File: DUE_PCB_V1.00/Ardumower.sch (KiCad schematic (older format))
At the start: 49 parts, among them J1 9V IN, J10 Sonar_R, J11 Sonar_C, J12 Sonar_L, J13 P_Right, J14 DS3231 RTC, J15 Button, J16 Button, J17 Button, J18 Button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

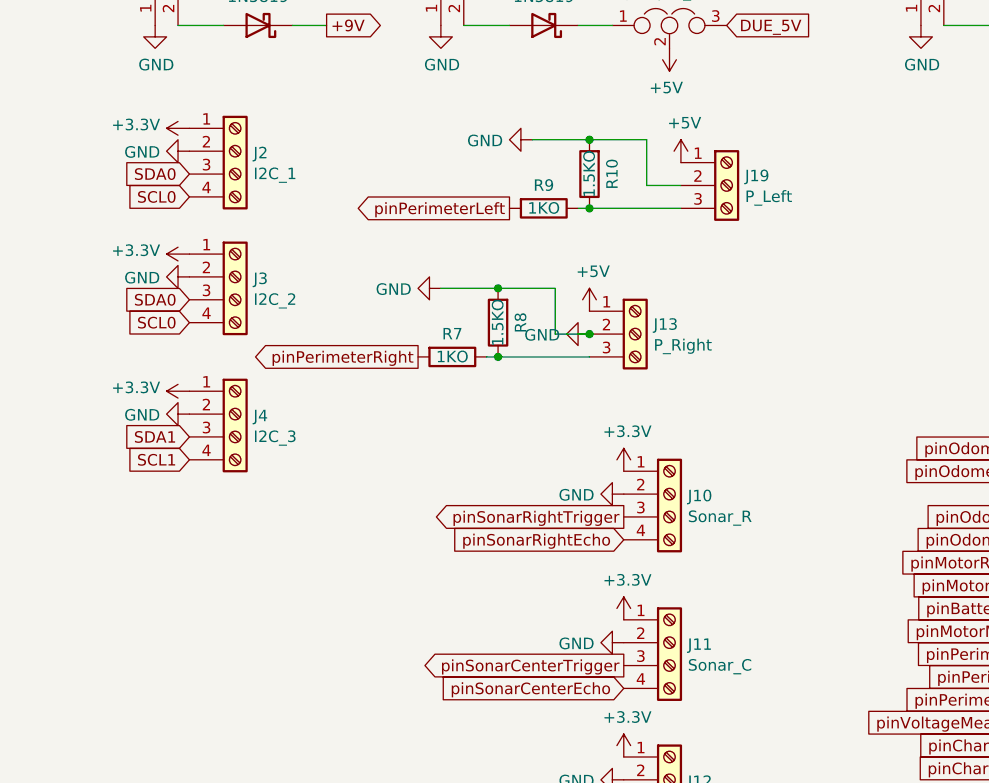
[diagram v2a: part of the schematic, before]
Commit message: Rename I2C Connectors
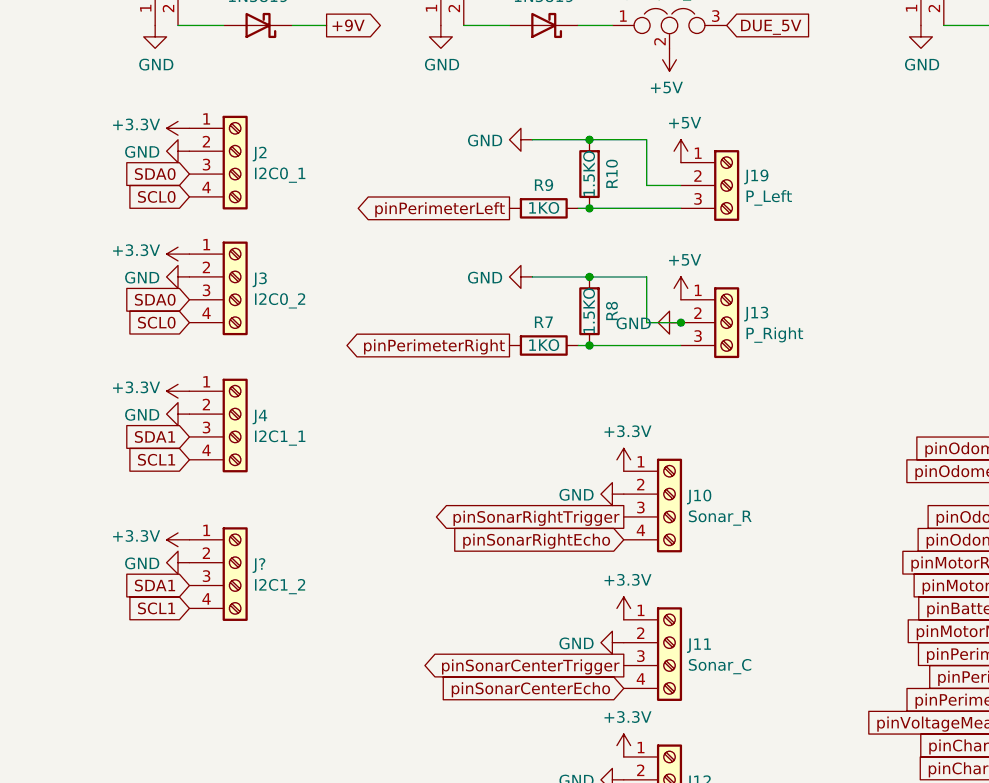
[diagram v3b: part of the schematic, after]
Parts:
- added J?: I2C1_2, Connector_PinHeader_2.54mm:PinHeader_1x04_P2.54mm_Vertical, symbol Connector:Screw_Terminal_01x04
- J2: value I2C_1 -> I2C0_1
- J3: value I2C_2 -> I2C0_2
- J4: value I2C_3 -> I2C1_1
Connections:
- net +3V3: now also J?.1 (Pin_1)
- net GND: now also J?.2 (Pin_2)
- net SCL1: now also J?.4 (Pin_4)
- net SDA1: now also J?.3 (Pin_3)
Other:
- moved on the sheet: J13, R7, R8
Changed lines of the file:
@@
 P 1150 1400
 F 0 "J2" H 1230 1392 50  0000 L CNN
-F 1 "I2C_1" H 1230 1301 50  0000 L CNN
+F 1 "I2C0_1" H 1230 1301 50  0000 L CNN
 F 2 "Connector_PinHeader_2.54mm:PinHeader_1x04_P2.54mm_Vertical" H 1150 1400 50  0001 C CNN
 F 3 "~" H 1150 1400 50  0001 C CNN
@@
 P 1150 1950
 F 0 "J3" H 1230 1942 50  0000 L CNN
-F 1 "I2C_2" H 1230 1851 50  0000 L CNN
+F 1 "I2C0_2" H 1230 1851 50  0000 L CNN
 F 2 "Connector_PinHeader_2.54mm:PinHeader_1x04_P2.54mm_Vertical" H 1150 1950 50  0001 C CNN
 F 3 "~" H 1150 1950 50  0001 C CNN
@@
 P 1150 2550
 F 0 "J4" H 1230 2542 50  0000 L CNN
-F 1 "I2C_3" H 1230 2451 50  0000 L CNN
+F 1 "I2C1_1" H 1230 2451 50  0000 L CNN
 F 2 "Connector_PinHeader_2.54mm:PinHeader_1x04_P2.54mm_Vertical" H 1150 2550 50  0001 C CNN
 F 3 "~" H 1150 2550 50  0001 C CNN
@@
 L Connector:Screw_Terminal_01x03 J13
 U 1 1 6077742A
-P 2900 2200
-F 0 "J13" H 2980 2242 50  0000 L CNN
-F 1 "P_Right" H 2980 2151 50  0000 L CNN
-F 2 "Connector_PinHeader_2.54mm:PinHeader_1x03_P2.54mm_Vertical" H 2900 2200 50  0001 C CNN
-F 3 "~" H 2900 2200 50  0001 C CNN
-	1    2900 2200
+P 3300 2150
+F 0 "J13" H 3380 2192 50  0000 L CNN
+F 1 "P_Right" H 3380 2101 50  0000 L CNN
+F 2 "Connector_PinHeader_2.54mm:PinHeader_1x03_P2.54mm_Vertical" H 3300 2150 50  0001 C CNN
+F 3 "~" H 3300 2150 50  0001 C CNN
+	1    3300 2150
 	1    0    0    -1
 $EndComp
@@
 L power:+5V #PWR026
 U 1 1 6077B973
-P 2700 2100
-F 0 "#PWR026" H 2700 1950 50  0001 C CNN
-F 1 "+5V" H 2715 2273 50  0000 C CNN
-F 2 "" H 2700 2100 50  0001 C CNN
-F 3 "" H 2700 2100 50  0001 C CNN
-	1    2700 2100
-	1    0    0    -1
-$EndComp
-Text GLabel 1950 2300 0    50   Output ~ 0
+P 3100 2050
+F 0 "#PWR026" H 3100 1900 50  0001 C CNN
+F 1 "+5V" H 3115 2223 50  0000 C CNN
+F 2 "" H 3100 2050 50  0001 C CNN
+F 3 "" H 3100 2050 50  0001 C CNN
+	1    3100 2050
+	1    0    0    -1
+$EndComp
+Text GLabel 2350 2250 0    50   Output ~ 0
 pinPerimeterRight
 $Comp
@@
 L power:GND #PWR027
 U 1 1 6097F899
-P 2700 2200
-F 0 "#PWR027" H 2700 1950 50  0001 C CNN
-F 1 "GND" V 2705 2072 50  0000 R CNN
-F 2 "" H 2700 2200 50  0001 C CNN
-F 3 "" H 2700 2200 50  0001 C CNN
-	1    2700 2200
+P 3100 2150
+F 0 "#PWR027" H 3100 1900 50  0001 C CNN
+F 1 "GND" V 3105 2022 50  0000 R CNN
+F 2 "" H 3100 2150 50  0001 C CNN
+F 3 "" H 3100 2150 50  0001 C CNN
+	1    3100 2150
 	0    1    1    0
 $EndComp
@@
 L power:GND #PWR021
 U 1 1 6076CF93
-P 2050 2000
-F 0 "#PWR021" H 2050 1750 50  0001 C CNN
-F 1 "GND" V 2055 1872 50  0000 R CNN
-F 2 "" H 2050 2000 50  0001 C CNN
-F 3 "" H 2050 2000 50  0001 C CNN
-	1    2050 2000
-	0    1    1    0
-$EndComp
-Wire Wire Line
-	2550 2000 2550 2200
-Wire Wire Line
-	2550 2200 2700 2200
-Wire Wire Line
-	2550 2000 2300 2000
-Wire Wire Line
-	2050 2000 2300 2000
-Connection ~ 2300 2000
-Wire Wire Line
-	2700 2300 2300 2300
-Connection ~ 2300 2300
+P 2450 1950
+F 0 "#PWR021" H 2450 1700 50  0001 C CNN
+F 1 "GND" V 2455 1822 50  0000 R CNN
+F 2 "" H 2450 1950 50  0001 C CNN
+F 3 "" H 2450 1950 50  0001 C CNN
+	1    2450 1950
+	0    1    1    0
+$EndComp
+Wire Wire Line
+	2950 1950 2950 2150
+Wire Wire Line
+	2950 2150 3100 2150
+Wire Wire Line
+	2950 1950 2700 1950
+Wire Wire Line
+	2450 1950 2700 1950
+Connection ~ 2700 1950
+Wire Wire Line
+	3100 2250 2700 2250
+Connection ~ 2700 2250
 $Comp
 L Device:R R8
 U 1 1 6076D98E
-P 2300 2150
-F 0 "R8" V 2200 2150 50  0000 C CNN
-F 1 "1.5KO" V 2300 2150 50  0000 C CNN
-F 2 "Resistor_THT:R_Axial_DIN0207_L6.3mm_D2.5mm_P2.54mm_Vertical" V 2230 2150 50  0001 C CNN
-F 3 "~" H 2300 2150 50  0001 C CNN
-	1    2300 2150
+P 2700 2100
+F 0 "R8" V 2600 2100 50  0000 C CNN
+F 1 "1.5KO" V 2700 2100 50  0000 C CNN
+F 2 "Resistor_THT:R_Axial_DIN0207_L6.3mm_D2.5mm_P2.54mm_Vertical" V 2630 2100 50  0001 C CNN
+F 3 "~" H 2700 2100 50  0001 C CNN
+	1    2700 2100
 	-1   0    0    1
 $EndComp
 Wire Wire Line
-	2250 2300 2300 2300
+	2650 2250 2700 2250
 $Comp
 L Device:R R7
 U 1 1 6076D999
-P 2100 2300
-F 0 "R7" V 2000 2300 50  0000 C CNN
-F 1 "1KO" V 2100 2300 50  0000 C CNN
-F 2 "Resistor_THT:R_Axial_DIN0207_L6.3mm_D2.5mm_P2.54mm_Vertical" V 2030 2300 50  0001 C CNN
-F 3 "~" H 2100 2300 50  0001 C CNN
-	1    2100 2300
-	0    1    1    0
-$EndComp
-Connection ~ 2700 2200
+P 2500 2250
+F 0 "R7" V 2400 2250 50  0000 C CNN
+F 1 "1KO" V 2500 2250 50  0000 C CNN
+F 2 "Resistor_THT:R_Axial_DIN0207_L6.3mm_D2.5mm_P2.54mm_Vertical" V 2430 2250 50  0001 C CNN
+F 3 "~" H 2500 2250 50  0001 C CNN
+	1    2500 2250
+	0    1    1    0
+$EndComp
+Connection ~ 3100 2150
 $Comp
 L Connector:Screw_Terminal_01x06 J21
@@
 	1    0    0    -1
 $EndComp
+$Comp
+L Connector:Screw_Terminal_01x04 J?
+U 1 1 60CEE03C
+P 1150 3200
+F 0 "J?" H 1230 3192 50  0000 L CNN
+F 1 "I2C1_2" H 1230 3101 50  0000 L CNN
+F 2 "Connector_PinHeader_2.54mm:PinHeader_1x04_P2.54mm_Vertical" H 1150 3200 50  0001 C CNN
+F 3 "~" H 1150 3200 50  0001 C CNN
+	1    1150 3200
+	1    0    0    -1
+$EndComp
+Text GLabel 950  3300 0    50   Input ~ 0
+SDA1
+Text GLabel 950  3400 0    50   Input ~ 0
+SCL1
+$Comp
+L power:GND #PWR?
+U 1 1 60CEE9FC
+P 950 3200
+F 0 "#PWR?" H 950 2950 50  0001 C CNN
+F 1 "GND" V 955 3072 50  0000 R CNN
+F 2 "" H 950 3200 50  0001 C CNN
+F 3 "" H 950 3200 50  0001 C CNN
+	1    950  3200
+	0    1    1    0
+$EndComp
+$Comp
+L power:+3.3V #PWR?
+U 1 1 60CEEA06
+P 950 3100
+F 0 "#PWR?" H 950 2950 50  0001 C CNN
+F 1 "+3.3V" V 965 3228 50  0000 L CNN
+F 2 "" H 950 3100 50  0001 C CNN
+F 3 "" H 950 3100 50  0001 C CNN
+	1    950  3100
+	0    -1   -1   0
+$EndComp
 $EndSCHEMATC

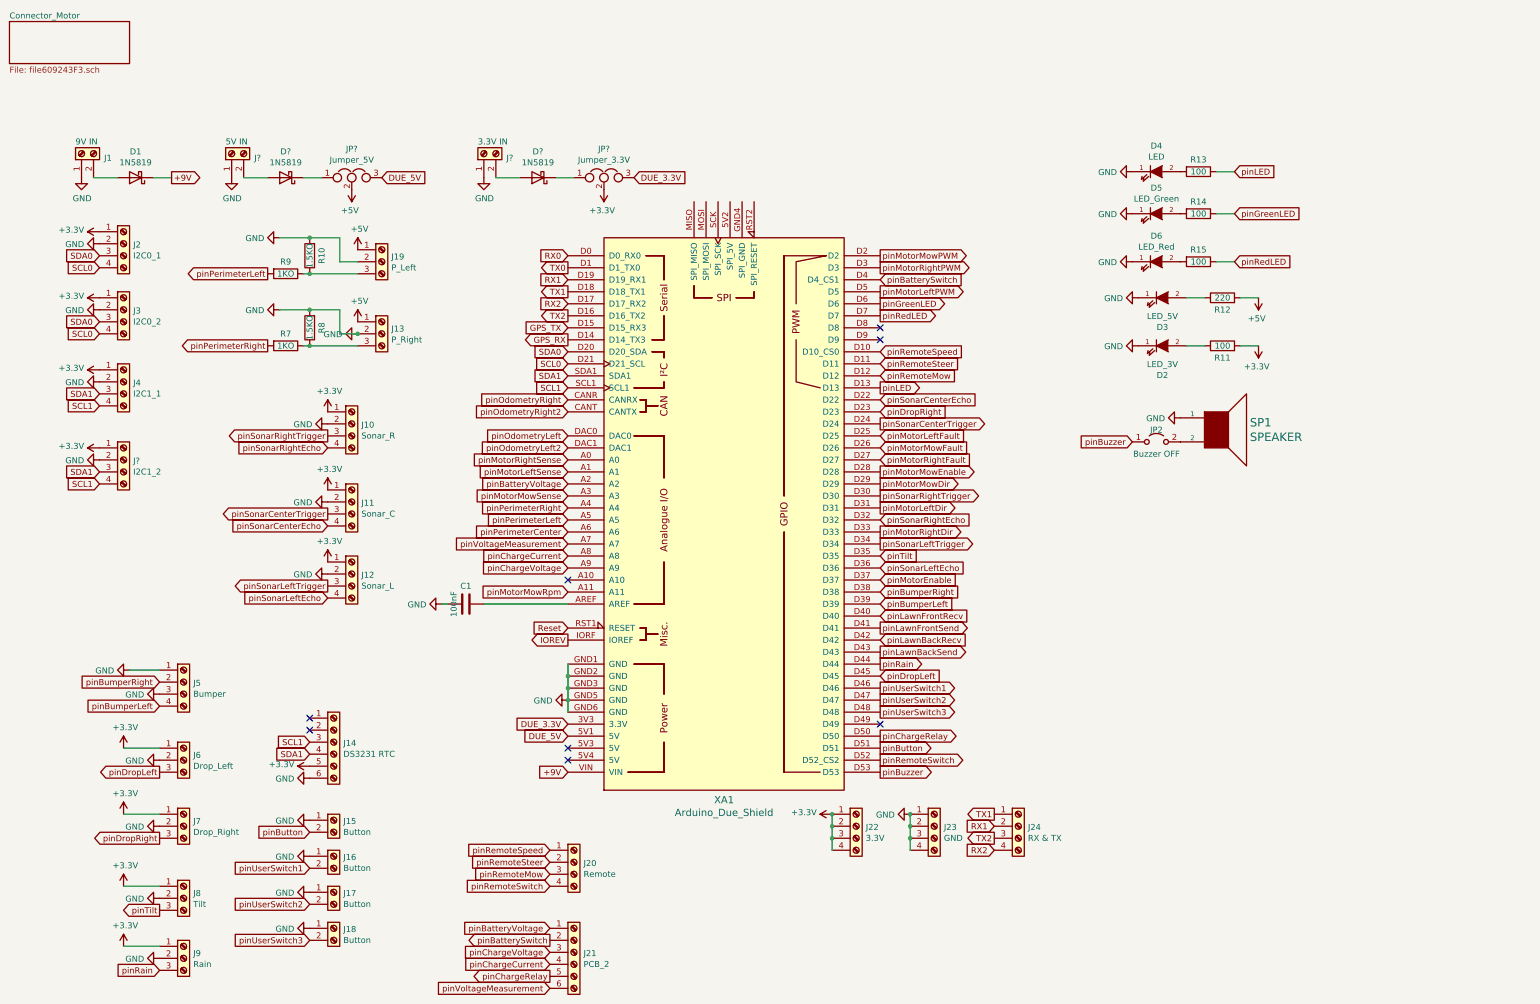
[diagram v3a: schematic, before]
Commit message: Add Pullup to I2C
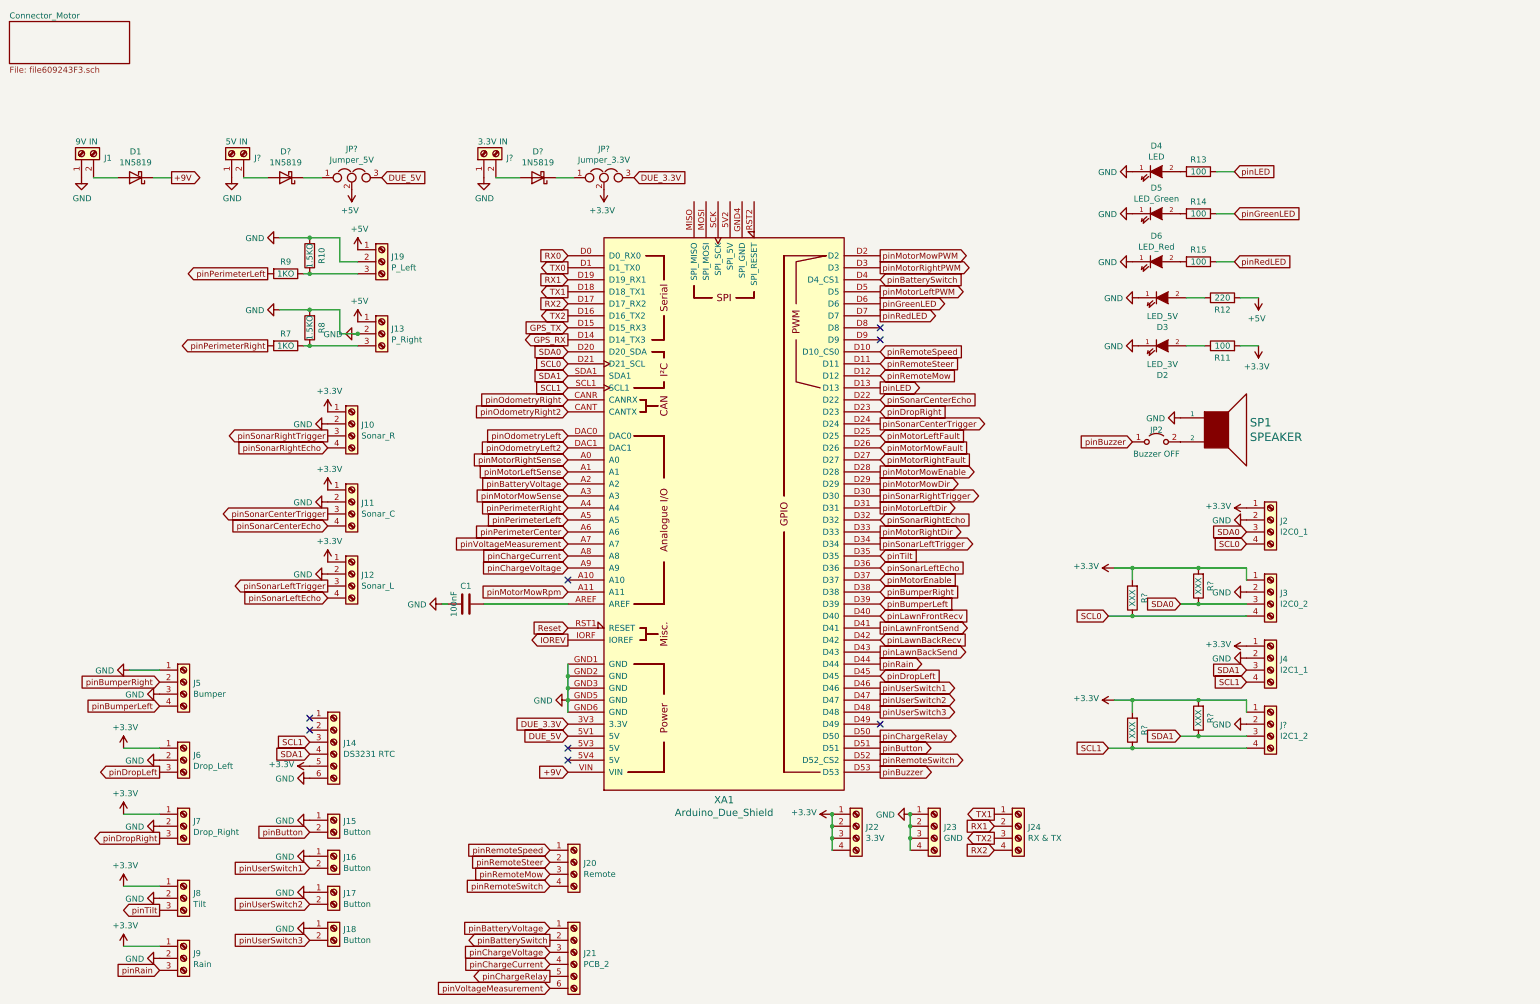
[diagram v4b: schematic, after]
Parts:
- removed J?: I2C1_2, Connector_PinHeader_2.54mm:PinHeader_1x04_P2.54mm_Vertical, symbol Connector:Screw_Terminal_01x04
- added J?: I2C1_2, Connector_PinHeader_2.54mm:PinHeader_1x04_P2.54mm_Vertical, symbol Connector:Screw_Terminal_01x04
- added R? (x4): XXX, Resistor_THT:R_Axial_DIN0207_L6.3mm_D2.5mm_P2.54mm_Vertical, symbol Device:R
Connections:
- net +3V3: now also J?.1 (Pin_1), R?.2, R?.2, R?.2, R?.2
- net GND: now also J?.2 (Pin_2)
- net SCL0: now also R?.1
- net SCL1: now also J?.4 (Pin_4), R?.1
- net SDA0: now also R?.1
- net SDA1: now also J?.3 (Pin_3), R?.1
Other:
- moved on the sheet: J2, J3, J4
